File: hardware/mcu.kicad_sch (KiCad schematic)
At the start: 22 parts, among them J301 TagConnect, J302 USER CONN., SW301 USER, U301 STM32G431, U302 SN65HVD230, Y301 12MHz

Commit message: update documentation
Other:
- note added: "I2C1_SDA"
- note added: "I2C3_SCL, DIR"
- note added: "I2C3_SDA, UART3_RX, STEP"
- note added: "MT6835 ABI"
- note added: "MT6835 SPI"
- note added: "UART3_TX, DIR"
- note removed: "really acting as UART3"
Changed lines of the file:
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@@
     (stroke (width 0) (type default))
+  )
+  (polyline (pts (xy 135.89 88.9) (xy 135.89 83.82))
+    (stroke (width 0) (type dash))
   )
   (wire (pts (xy 153.67 73.66) (xy 153.67 76.2))
@@
     (stroke (width 0) (type default))
   )
+  (polyline (pts (xy 50.8 116.84) (xy 50.8 121.92))
+    (stroke (width 0) (type dash))
+  )
   (wire (pts (xy 153.67 83.82) (xy 153.67 86.36))
     (stroke (width 0) (type default))
@@
     (stroke (width 0) (type default))
   )
+  (polyline (pts (xy 50.8 121.92) (xy 52.07 121.92))
+    (stroke (width 0) (type dash))
+  )
   (wire (pts (xy 38.1 154.94) (xy 38.1 156.21))
     (stroke (width 0) (type default))
@@
     (stroke (width 0) (type default))
   )
+  (polyline (pts (xy 134.62 88.9) (xy 135.89 88.9))
+    (stroke (width 0) (type dash))
+  )
+  (polyline (pts (xy 52.07 116.84) (xy 50.8 116.84))
+    (stroke (width 0) (type dash))
+  )
   (wire (pts (xy 199.39 35.56) (xy 199.39 38.1))
     (stroke (width 0) (type default))
@@
     (stroke (width 0) (type default))
   )
-  (text "I2C1_SCL" (at 123.19 110.49 0)
+  (polyline (pts (xy 135.89 83.82) (xy 134.62 83.82))
+    (stroke (width 0) (type dash))
+  )
+  (text "MT6835\nABI" (at 49.53 121.92 0)
+    (effects (font (size 1.27 1.27)) (justify right bottom))
+  )
+  (text "I2C3_SDA, UART3_RX, STEP" (at 59.69 97.79 0)
+    (effects (font (size 1.27 1.27)) (justify right bottom))
+  )
+  (text "I2C1_SDA\n" (at 64.77 127 0)
+    (effects (font (size 1.27 1.27)) (justify right bottom))
+  )
+  (text "I2C1_SCL" (at 121.92 109.22 0)
     (effects (font (size 1.27 1.27)) (justify left bottom))
   )
-  (text "really acting as UART3" (at 38.1 93.98 0)
+  (text "MT6835\nSPI" (at 137.16 87.63 0)
     (effects (font (size 1.27 1.27)) (justify left bottom))
   )
+  (text "I2C3_SCL, DIR" (at 133.35 92.71 0)
+    (effects (font (size 1.27 1.27)) (justify left bottom))
+  )
+  (text "UART3_TX, DIR" (at 45.72 95.25 0)
+    (effects (font (size 1.27 1.27)) (justify left bottom))
+  )

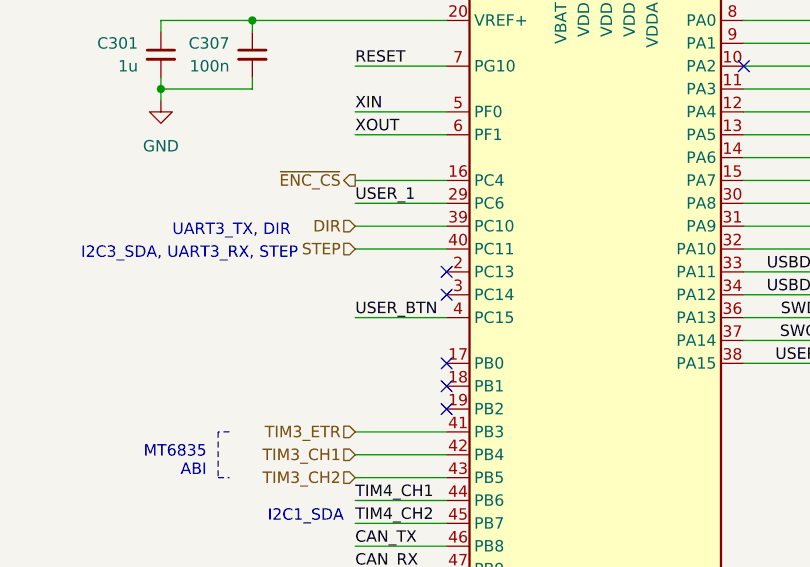
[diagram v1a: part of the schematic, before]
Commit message: Made analog gain of current sense amps selectable by mcu. Removed analog ground plane and tied all grounds together
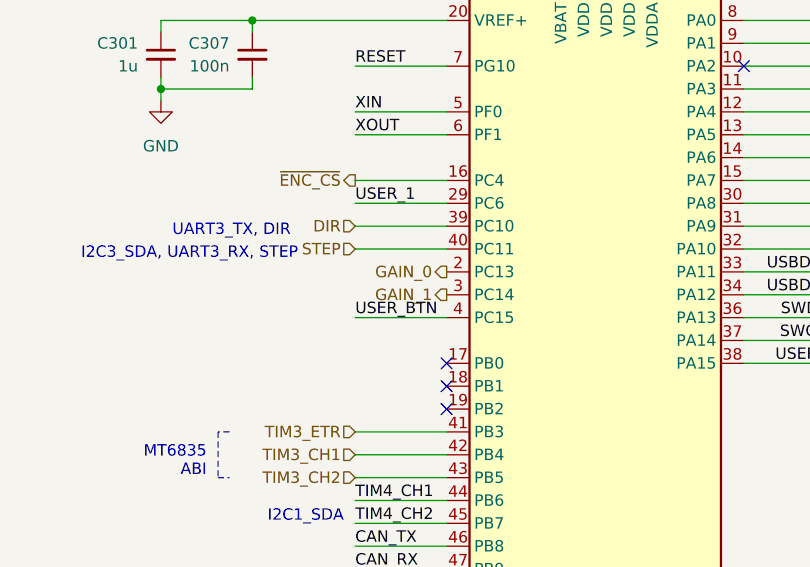
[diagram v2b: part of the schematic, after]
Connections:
- net GAIN_0: now reaches U301.2 (PC13)
- net GAIN_1: now reaches U301.3 (PC14)
- no-connect marks 9 -> 7
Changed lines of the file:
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@@
   (no_connect (at 243.84 50.8))
   (no_connect (at 109.22 76.2))
-  (no_connect (at 76.2 101.6))
   (no_connect (at 76.2 109.22))
   (no_connect (at 189.23 48.26))
   (no_connect (at 88.9 66.04))
-  (no_connect (at 76.2 99.06))
   (no_connect (at 76.2 111.76))
   (no_connect (at 76.2 114.3))
@@
     (effects (font (size 1.27 1.27)) (justify right))
   )
+  (hierarchical_label "GAIN_0" (shape output) (at 76.2 99.06 180) (fields_autoplaced)
+    (effects (font (size 1.27 1.27)) (justify right))
+  )
   (hierarchical_label "TIM3_CH2" (shape input) (at 66.04 121.92 180) (fields_autoplaced)
     (effects (font (size 1.27 1.27)) (justify right))
   )
+  (hierarchical_label "GAIN_1" (shape output) (at 76.2 101.6 180) (fields_autoplaced)
+    (effects (font (size 1.27 1.27)) (justify right))
+  )

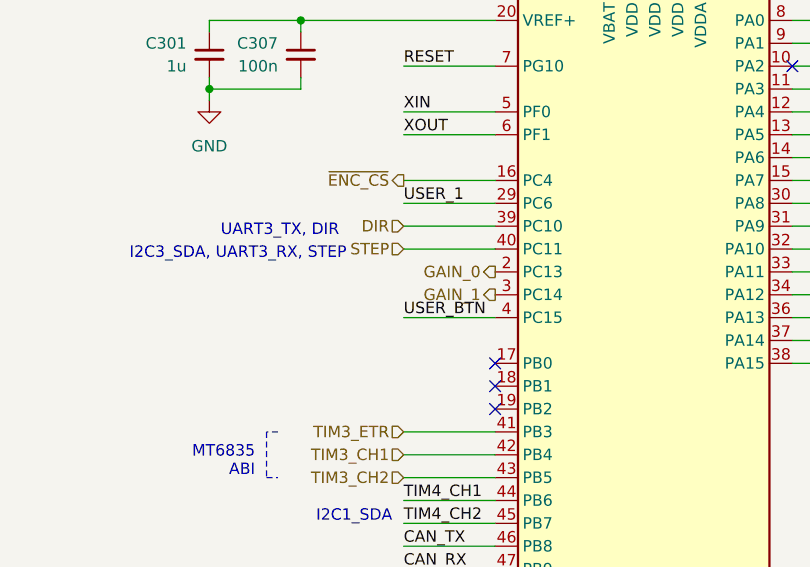
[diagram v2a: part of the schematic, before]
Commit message: Update firmware defines to match hardware
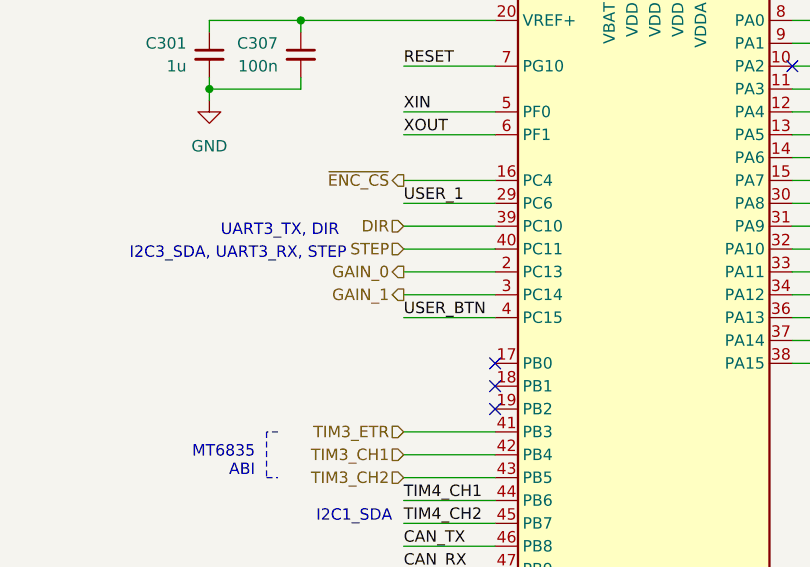
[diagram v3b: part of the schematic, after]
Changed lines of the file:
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@@
+    (stroke (width 0) (type default))
+  )
+  (wire (pts (xy 66.04 99.06) (xy 76.2 99.06))
     (stroke (width 0) (type default))
   )
@@
     (stroke (width 0) (type default))
   )
+  (wire (pts (xy 66.04 101.6) (xy 76.2 101.6))
+    (stroke (width 0) (type default))
+  )
   (wire (pts (xy 99.06 52.07) (xy 99.06 66.04))
     (stroke (width 0) (type default))
@@
     (effects (font (size 1.27 1.27)) (justify right))
   )
-  (hierarchical_label "GAIN_0" (shape output) (at 76.2 99.06 180) (fields_autoplaced)
+  (hierarchical_label "GAIN_0" (shape output) (at 66.04 99.06 180) (fields_autoplaced)
     (effects (font (size 1.27 1.27)) (justify right))
   )
@@
     (effects (font (size 1.27 1.27)) (justify right))
   )
-  (hierarchical_label "GAIN_1" (shape output) (at 76.2 101.6 180) (fields_autoplaced)
-    (effects (font (size 1.27 1.27)) (justify right))
-  )
+  (hierarchical_label "GAIN_1" (shape output) (at 66.04 101.6 180) (fields_autoplaced)
+    (effects (font (size 1.27 1.27)) (justify right))
+  )

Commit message: Update BOM field LCSC ID
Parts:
- C301: LCSC ID (none) -> C52923; LCSC Part C52923 -> (none)
- C302, C303, C304, C307, C308: LCSC ID (none) -> C307331; LCSC Part C307331 -> (none)
- C305, C306: LCSC ID (none) -> C1554; LCSC Part C1554 -> (none)
- D301: LCSC ID (none) -> C72041; LCSC Part C72041 -> (none)
- D302: LCSC ID (none) -> C2286; LCSC Part C2286 -> (none)
- R301, R302: LCSC ID (none) -> C25905; LCSC Part C25905 -> (none)
- R303: LCSC ID (none) -> C25794; LCSC Part C25794 -> (none)
- R304: LCSC ID (none) -> C25890; LCSC Part C25890 -> (none)
- R305, R306: LCSC ID (none) -> C25744; LCSC Part C25744 -> (none)
- SW301: LCSC ID (none) -> C963349; LCSC Part C963349 -> (none)
- U301: LCSC ID (none) -> C529356; LCSC Part C529356 -> (none)
- U302: LCSC ID (none) -> C12084; LCSC Part C12084 -> (none)
- Y301: LCSC ID (none) -> C9002; LCSC Part C9002 -> (none)
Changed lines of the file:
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@@
 			)
 		)
-		(property "LCSC Part" "C25744"
+		(property "LCSC ID" "C25744"
 			(at 254 86.36 0)
 			(effects
@@
 			)
 		)
-		(property "LCSC Part" "C9002"
+		(property "LCSC ID" "C9002"
 			(at 196.85 90.17 0)
 			(effects
@@
 			)
 		)
-		(property "LCSC Part" "C1554"
+		(property "LCSC ID" "C1554"
 			(at 186.69 96.52 0)
 			(effects
@@
 			)
 		)
-		(property "LCSC Part" "C25905"
+		(property "LCSC ID" "C25905"
 			(at 25.4 143.51 0)
 			(effects
@@
 			)
 		)
-		(property "LCSC Part" "C307331"
+		(property "LCSC ID" "C307331"
 			(at 143.51 55.88 0)
 			(effects
@@
 			)
 		)
-		(property "LCSC Part" "C2286"
+		(property "LCSC ID" "C2286"
 			(at 38.1 151.13 0)
 			(effects
@@
 			)
 		)
-		(property "LCSC Part" "C307331"
+		(property "LCSC ID" "C307331"
 			(at 123.19 55.88 0)
 			(effects
@@
 			)
 		)
-		(property "LCSC Part" "C307331"
+		(property "LCSC ID" "C307331"
 			(at 133.35 55.88 0)
 			(effects
@@
 			)
 		)
-		(property "LCSC Part" "C963349"
+		(property "LCSC ID" "C963349"
 			(at 208.28 134.62 0)
 			(effects
@@
 			)
 		)
-		(property "LCSC Part" "C52923"
+		(property "LCSC ID" "C52923"
 			(at 44.45 74.93 0)
 			(effects
@@
 			)
 		)
-		(property "LCSC Part" "C307331"
+		(property "LCSC ID" "C307331"
 			(at 54.61 74.93 0)
 			(effects
@@
 			)
 		)
-		(property "LCSC Part" "C529356"
+		(property "LCSC ID" "C529356"
 			(at 91.44 111.76 0)
 			(effects
@@
 			)
 		)
-		(property "LCSC Part" "C25744"
+		(property "LCSC ID" "C25744"
 			(at 200.66 142.24 0)
 			(effects
@@
 			)
 		)
-		(property "LCSC Part" "C25794"
+		(property "LCSC ID" "C25794"
 			(at 153.67 71.12 0)
 			(effects
@@
 			)
 		)
-		(property "LCSC Part" "C25905"
+		(property "LCSC ID" "C25905"
 			(at 38.1 143.51 0)
 			(effects
@@
 			)
 		)
-		(property "LCSC Part" "C72041"
+		(property "LCSC ID" "C72041"
 			(at 25.4 151.13 0)
 			(effects
@@
 			)
 		)
-		(property "LCSC Part" "C12084"
+		(property "LCSC ID" "C12084"
 			(at 199.39 45.72 0)
 			(effects
@@
 			)
 		)
-		(property "LCSC Part" "C25890"
+		(property "LCSC ID" "C25890"
 			(at 153.67 81.28 0)
 			(effects
@@
 			)
 		)
-		(property "LCSC Part" "C307331"
+		(property "LCSC ID" "C307331"
 			(at 254 93.98 0)
 			(effects
@@
 			)
 		)
-		(property "LCSC Part" "C1554"
+		(property "LCSC ID" "C1554"
 			(at 207.01 96.52 0)
 			(effects

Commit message: fix BOM to use basic parts again
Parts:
- D301: LCSC ID C72041 -> C2290
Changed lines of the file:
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@@
 			)
 		)
-		(property "LCSC ID" "C72041"
+		(property "LCSC ID" "C2290"
 			(at 25.4 151.13 0)
 			(effects

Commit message: clean erc drc, pack sym, footprints into standalone lib
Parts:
- C301, C302, C303, C304, C305, C306, C307, C308: footprint Capacitor_SMD:C_0402_1005Metric -> lemon-pepper-footprints:C_0402_1005Metric; symbol Device:C_Small -> lemon-pepper-symbols:C_Small
- D301, D302: footprint Diode_SMD:D_0603_1608Metric -> lemon-pepper-footprints:D_0603_1608Metric; symbol Device:LED -> lemon-pepper-symbols:LED
- J301: symbol Connector:Conn_ARM_SWD_TagConnect_TC2030-NL -> lemon-pepper-symbols:Conn_ARM_SWD_TagConnect_TC2030-NL
- J302: footprint mechanical:PinHeader_1x05_P1.27mm_SMD -> lemon-pepper-footprints:PinHeader_1x05_P1.27mm_SMD; symbol Connector_Generic:Conn_01x05 -> lemon-pepper-symbols:Conn_01x05
- R301, R302, R303, R304, R305, R306: footprint Resistor_SMD:R_0402_1005Metric -> lemon-pepper-footprints:R_0402_1005Metric; symbol Device:R_Small_US -> lemon-pepper-symbols:R_Small_US
- SW301: footprint Button_Switch_SMD:SW_SPST_B3U-3000P -> lemon-pepper-footprints:SW_SPST_B3U-3000P; symbol Switch:SW_Push_45deg -> lemon-pepper-symbols:SW_Push_45deg
- U301: footprint Package_DFN_QFN:QFN-48-1EP_7x7mm_P0.5mm_EP5.6x5.6mm -> lemon-pepper-footprints:QFN-48-1EP_7x7mm_P0.5mm_EP5.6x5.6mm; symbol MCU_ST_STM32G4:STM32G431CBUx -> lemon-pepper-symbols:STM32G431CBUx
- U302: footprint Package_SO:SOIC-8_3.9x4.9mm_P1.27mm -> lemon-pepper-footprints:SOIC-8_3.9x4.9mm_P1.27mm; symbol Interface_CAN_LIN:SN65HVD230 -> lemon-pepper-symbols:SN65HVD230
- Y301: footprint Crystal:Crystal_SMD_3225-4Pin_3.2x2.5mm -> lemon-pepper-footprints:Crystal_SMD_3225-4Pin_3.2x2.5mm; symbol Device:Crystal_GND24 -> lemon-pepper-symbols:Crystal_GND24
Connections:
- no-connect marks 7 -> 6
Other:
- moved on the sheet: C301, C307, D301, D302, R301, R302, R303, R304, U301
